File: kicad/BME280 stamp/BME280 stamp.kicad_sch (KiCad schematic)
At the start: 5 parts, among them U1 BME280

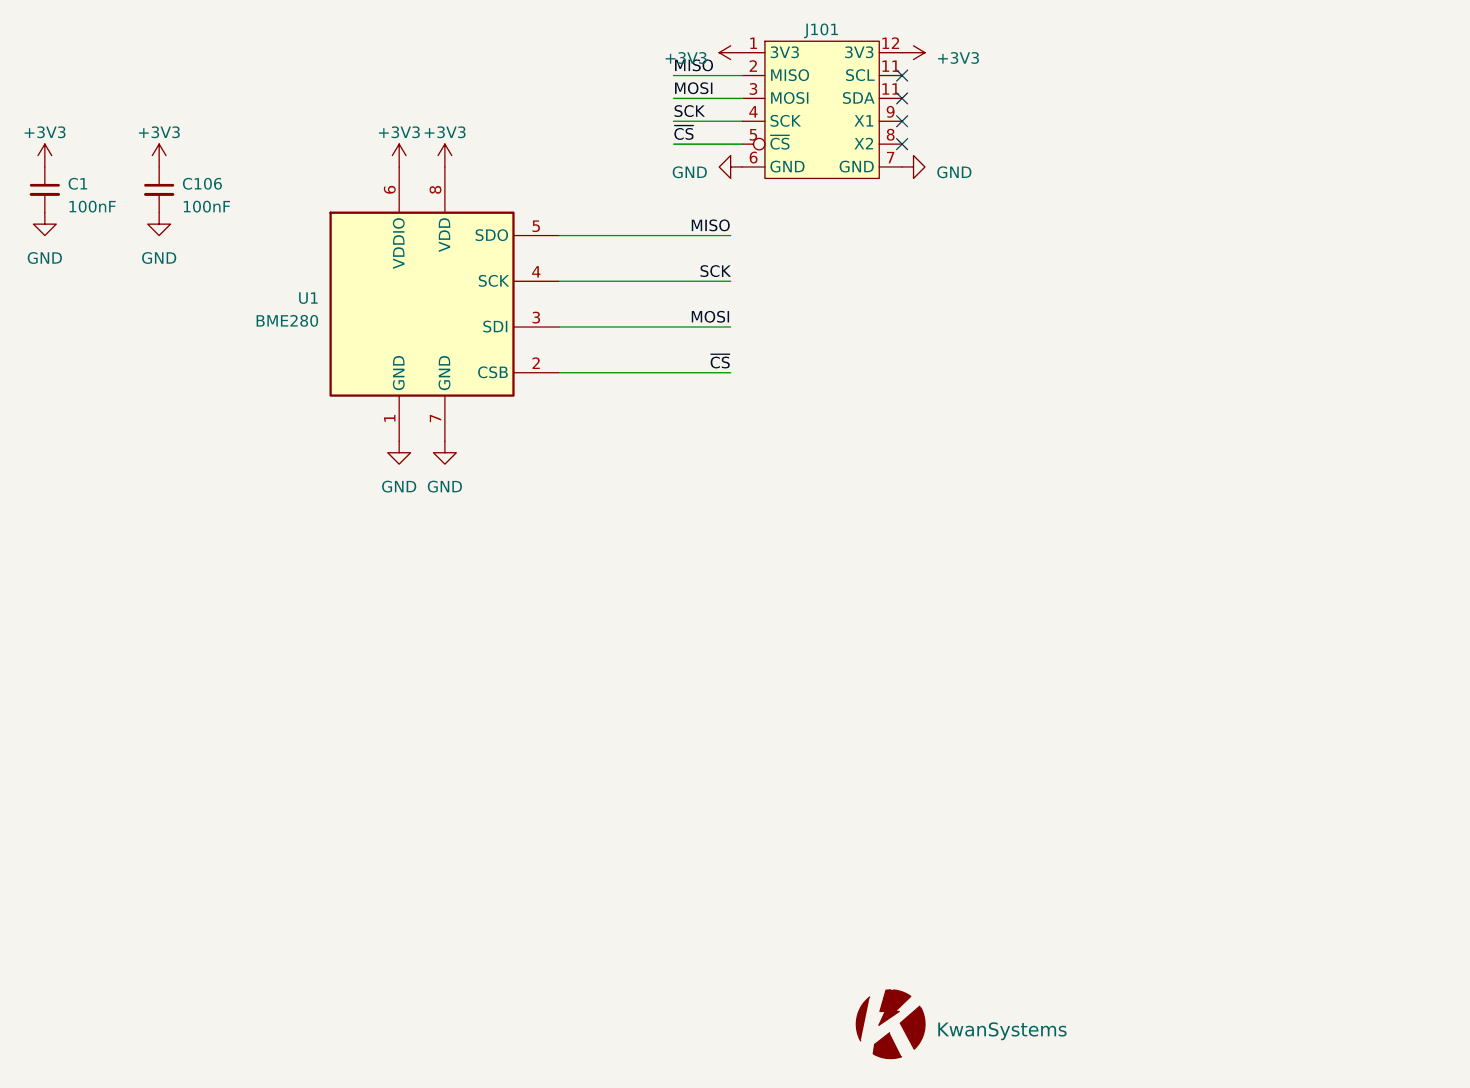
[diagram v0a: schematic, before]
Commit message: Added labels to BME280 stamp
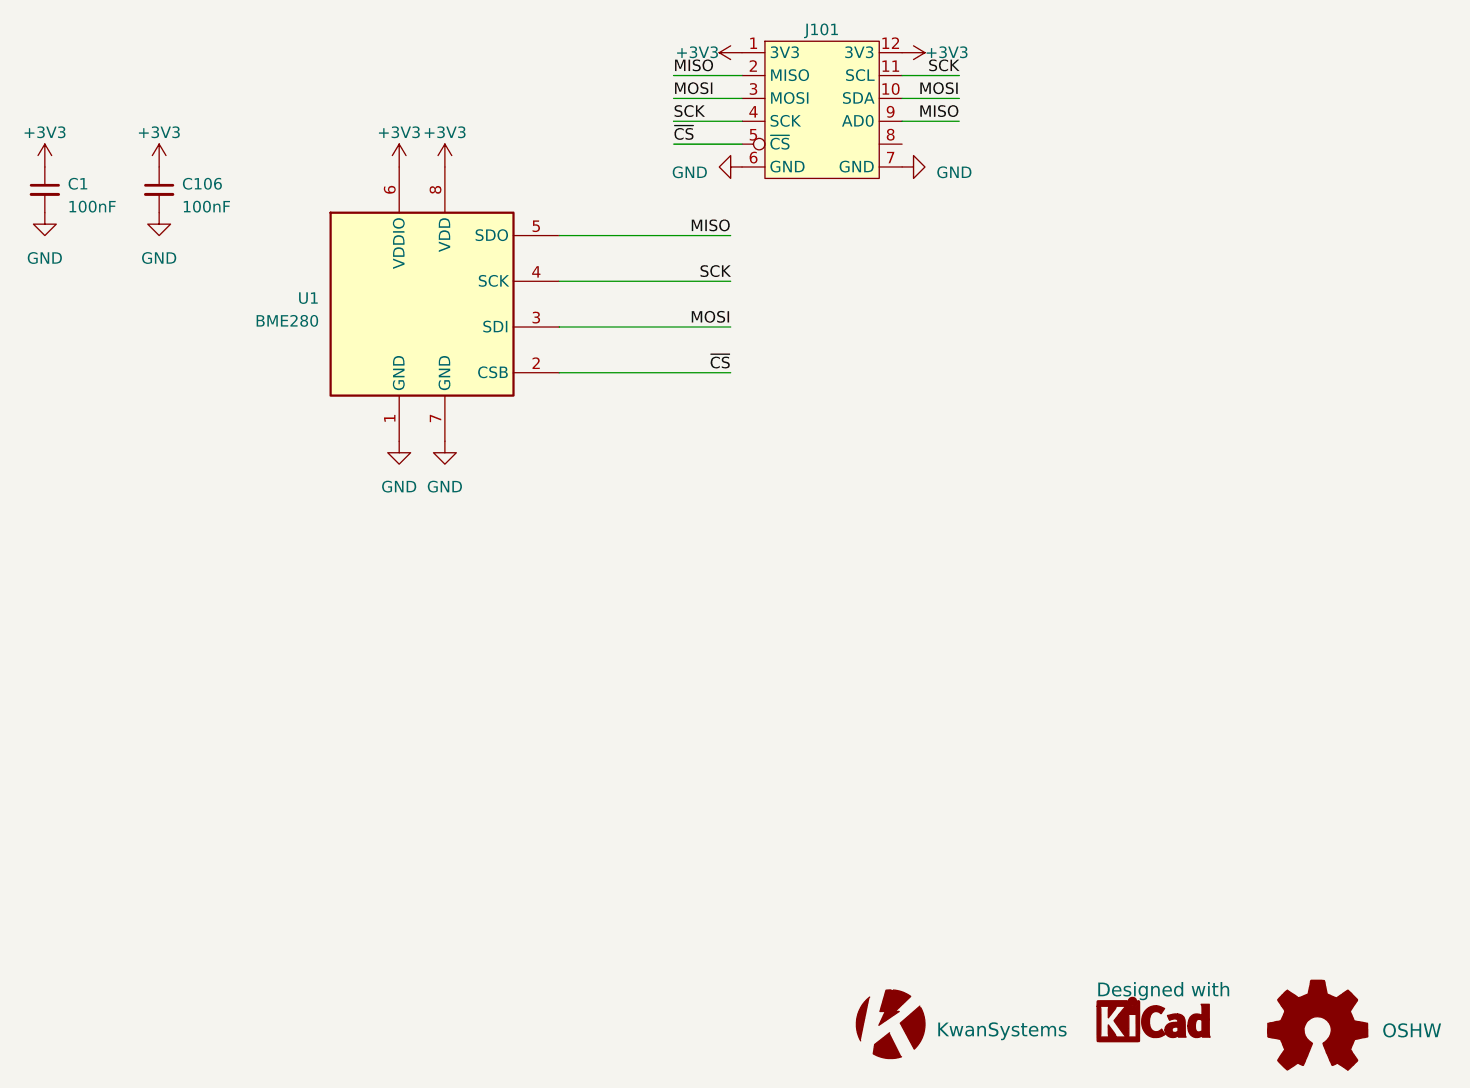
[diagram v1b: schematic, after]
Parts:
- added G2: Designed with, KwanSystems:Symbol_KiCAD-Logo_CopperAndSilkScreenTop_small, symbol KwanSystems:DesignedWithKicad
- added G3: OSHW, KwanSystems:OSHW-Symbol_4x3.6mm_SolderMask, symbol KwanSystems:OSHW
- G1: footprint KwanSystems:StKwansSoldermask -> KwanSystems:KWAN_CIRCLE
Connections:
- net MISO: now also J101.9 (AD0)
- net MOSI: now also J101.10 (SDA)
- net SCK: now also J101.11 (SCL)
- no-connect marks 4 -> 0
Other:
- company: (none) -> Kwan Systems
- title: (none) -> BME280 Stamp
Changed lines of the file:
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@@
 (kicad_sch (version 20230121) (generator eeschema)
   (paper "A4")
-  (no_connect (at 184.15 73.66))
-  (no_connect (at 184.15 66.04))
-  (no_connect (at 184.15 68.58))
-  (no_connect (at 184.15 71.12))
+  (title_block
+    (title "BME280 Stamp")
+    (date "2023-03-23")
+    (company "Kwan Systems")
+  )
   (wire (pts (xy 146.05 88.9) (xy 165.1 88.9))
     (stroke (width 0) (type default))
@@
     (stroke (width 0) (type default))
   )
+  (wire (pts (xy 184.15 66.04) (xy 190.5 66.04))
+    (stroke (width 0) (type default))
+  )
   (wire (pts (xy 166.37 68.58) (xy 158.75 68.58))
     (stroke (width 0) (type default))
@@
     (stroke (width 0) (type default))
   )
+  (wire (pts (xy 184.15 71.12) (xy 190.5 71.12))
+    (stroke (width 0) (type default))
+  )
   (wire (pts (xy 166.37 71.12) (xy 158.75 71.12))
+    (stroke (width 0) (type default))
+  )
+  (wire (pts (xy 184.15 68.58) (xy 190.5 68.58))
     (stroke (width 0) (type default))
   )
@@
     (effects (font (size 1.27 1.27)) (justify left bottom))
   )
+  (label "MOSI" (at 190.5 68.58 180) (fields_autoplaced)
+    (effects (font (size 1.27 1.27)) (justify right bottom))
+  )
   (label "SCK" (at 158.75 71.12 0) (fields_autoplaced)
     (effects (font (size 1.27 1.27)) (justify left bottom))
@@
     (effects (font (size 1.27 1.27)) (justify left bottom))
   )
+  (label "MISO" (at 190.5 71.12 180) (fields_autoplaced)
+    (effects (font (size 1.27 1.27)) (justify right bottom))
+  )
   (label "MOSI" (at 165.1 93.98 180) (fields_autoplaced)
+    (effects (font (size 1.27 1.27)) (justify right bottom))
+  )
+  (label "SCK" (at 190.5 66.04 180) (fields_autoplaced)
     (effects (font (size 1.27 1.27)) (justify right bottom))
   )
@@
     (pin "1")
     (pin "11")
-    (pin "11")
+    (pin "10")
     (pin "12")
     (pin "2")
@@
   )
   (symbol (lib_id "power:+3V3") (at 184.15 63.5 270) (mirror x) (unit 1)
-    (in_bom yes) (on_board yes) (dnp no) (fields_autoplaced)
+    (in_bom yes) (on_board yes) (dnp no)
     (property "Reference" "#PWR011" (at 180.34 63.5 0)
       (effects (font (size 1.27 1.27)) hide)
     )
-    (property "Value" "+3V3" (at 187.96 64.135 90)
+    (property "Value" "+3V3" (at 186.69 63.5 90)
       (effects (font (size 1.27 1.27)) (justify left))
     )
@@
         (path "/499b7167-cb0d-476d-babd-3d5f0a5ab153"
           (reference "C1") (unit 1)
+        )
+      )
+    )
+  )
+  (symbol (lib_id "KwanSystems:DesignedWithKicad") (at 212.09 172.72 0) (unit 1)
+    (in_bom no) (on_board yes) (dnp no)
+    (property "Reference" "G2" (at 212.09 175.26 0)
+      (effects (font (size 1.524 1.524)) hide)
+    )
+    (property "Value" "Designed with" (at 205.74 167.64 0)
+      (effects (font (size 1.524 1.524)) (justify left))
+    )
+    (property "Footprint" "KwanSystems:Symbol_KiCAD-Logo_CopperAndSilkScreenTop_small" (at 210.82 177.8 0)
+      (effects (font (size 1.524 1.524)) hide)
+    )
+    (property "Datasheet" "" (at 212.09 172.72 0)
+      (effects (font (size 1.524 1.524)) hide)
+    )
+    (instances
+      (project "BME280 stamp"
+        (path "/499b7167-cb0d-476d-babd-3d5f0a5ab153"
+          (reference "G2") (unit 1)
         )
       )
@@
       (effects (font (size 1.524 1.524)) (justify left))
     )
-    (property "Footprint" "KwanSystems:StKwansSoldermask" (at 182.88 166.37 0)
+    (property "Footprint" "KwanSystems:KWAN_CIRCLE" (at 182.88 166.37 0)
       (effects (font (size 1.524 1.524)) hide)
     )
@@
         (path "/499b7167-cb0d-476d-babd-3d5f0a5ab153"
           (reference "G1") (unit 1)
+        )
+      )
+    )
+  )
+  (symbol (lib_id "KwanSystems:OSHW") (at 229.87 172.72 0) (unit 1)
+    (in_bom no) (on_board yes) (dnp no) (fields_autoplaced)
+    (property "Reference" "G3" (at 238.76 173.99 0)
+      (effects (font (size 1.524 1.524)) hide)
+    )
+    (property "Value" "OSHW" (at 237.49 172.1866 0)
+      (effects (font (size 1.524 1.524)) (justify left))
+    )
+    (property "Footprint" "KwanSystems:OSHW-Symbol_4x3.6mm_SolderMask" (at 237.49 177.8 0)
+      (effects (font (size 1.524 1.524)) hide)
+    )
+    (property "Datasheet" "" (at 229.87 172.72 0)
+      (effects (font (size 1.524 1.524)) hide)
+    )
+    (instances
+      (project "BME280 stamp"
+        (path "/499b7167-cb0d-476d-babd-3d5f0a5ab153"
+          (reference "G3") (unit 1)
         )
       )
@@
   )
   (symbol (lib_id "power:+3V3") (at 166.37 63.5 90) (mirror x) (unit 1)
-    (in_bom yes) (on_board yes) (dnp no) (fields_autoplaced)
+    (in_bom yes) (on_board yes) (dnp no)
     (property "Reference" "#PWR09" (at 170.18 63.5 0)
       (effects (font (size 1.27 1.27)) hide)
     )
-    (property "Value" "+3V3" (at 162.56 64.135 90)
+    (property "Value" "+3V3" (at 163.83 63.5 90)
       (effects (font (size 1.27 1.27)) (justify left))
     )
